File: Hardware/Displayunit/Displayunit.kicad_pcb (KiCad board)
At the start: 4 copper layers, 155 x 64.8 mm, 112 parts, among them IC1 TSC2007, IC2 MX25LM51245GXDI00, IC3 IS66WVH8M8BLL-100B1LI_0, J1 8P8C_Shielded, J2 8P8C_Shielded, J3 54104-4031, J4 Conn_ARM_JTAG_SWD_20, J5 52271-0679, J6 Conn_02x06_Odd_Even, J7 734-264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

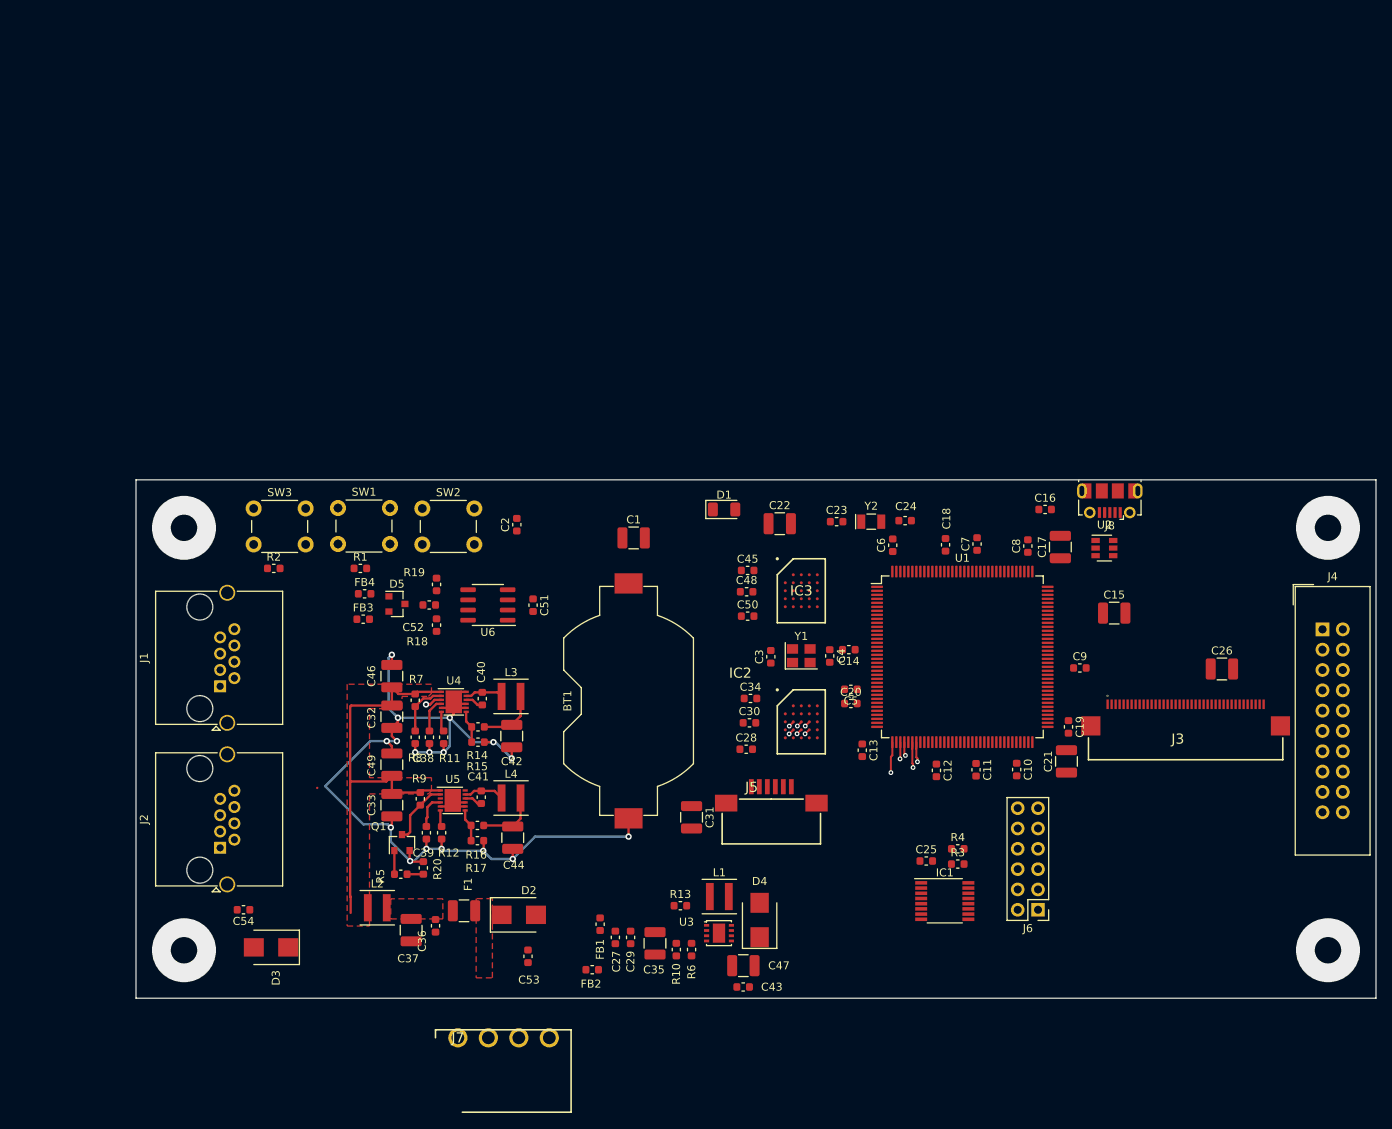
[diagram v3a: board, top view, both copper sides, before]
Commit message: Displayboard: Flex Stecker Position festgelegt, verschiebung von Componenten.
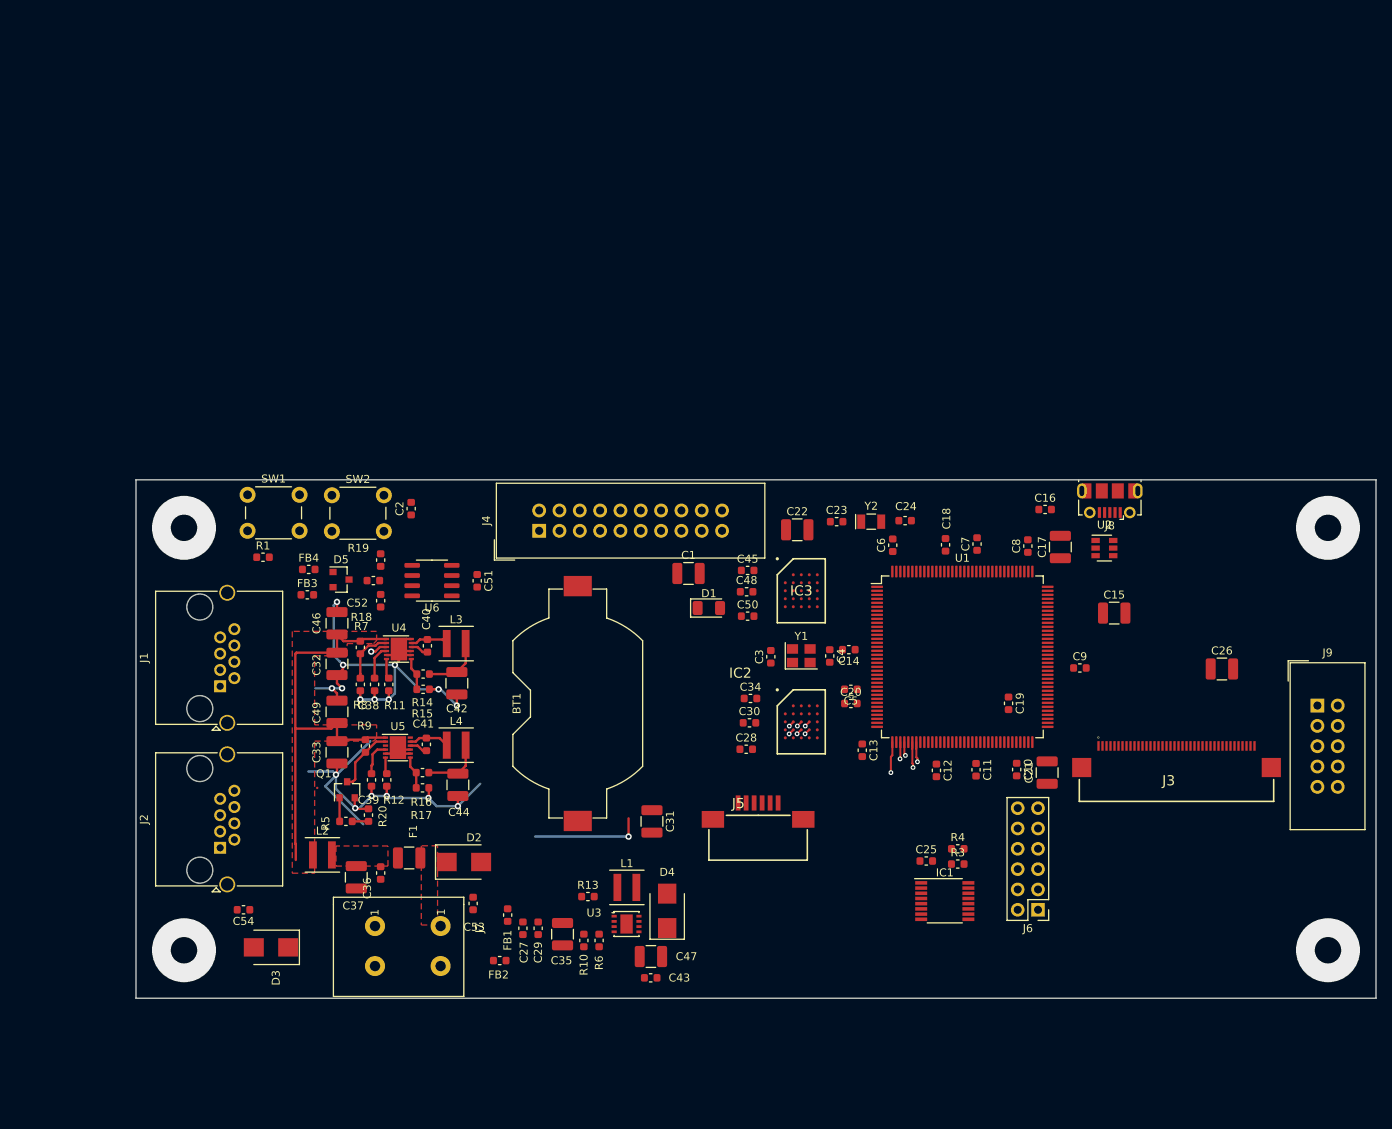
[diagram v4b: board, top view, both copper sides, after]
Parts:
- removed R2: 10K, Resistor_SMD:R_0603_1608Metric
- removed SW3: Wakeup, Button_Switch_THT:SW_PUSH_6mm_H8.5mm
- added J9: Conn_02x05_Odd_Even, Connector_IDC:IDC-Header_2x05_P2.54mm_Vertical, F.Cu at (209.7, 77.2)
- J7: value 734-264 -> WAGO_Klemmleiste_2-pol; footprint WAGO:SHDR4W120P0X381_1X4_1640X1030X850P -> WAGO:WAGO_Klemmleiste_Hebel4mm²Horizontal_RM5mm_2-pol
- moved J4 98.7 mm to (112.4, 55.4), turned to 90 degrees
- moved J7 14.1 mm to (100.1, 104.8), turned to 270 degrees
- moved C2 13.4 mm to (96.4, 52.6)
- moved D1 12.5 mm to (133.6, 65.0)
- moved R1 12.2 mm to (77.9, 58.7)
- moved C47 11.6 mm to (126.4, 108.6)
- moved D4 11.6 mm to (128.4, 102.9)
- moved C27 11.6 mm to (110.4, 105.1)
- moved C29 11.6 mm to (112.3, 105.1)
- moved C35 11.6 mm to (115.3, 105.8)
- moved C43 11.6 mm to (126.3, 111.3)
- moved FB1 11.6 mm to (108.5, 103.4)
- moved FB2 11.6 mm to (107.5, 109.1)
- moved L1 11.6 mm to (123.4, 99.9)
- moved R13 11.6 mm to (118.5, 101.1)
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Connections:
- J7 pad 2: Net-(C53-Pad1) -> GND

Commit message: Displayboard: Layout
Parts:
- added C55: 1uF, Capacitor_SMD:C_1210_3225Metric, F.Cu at (212.9, 68.7)
- added C56: 100n, Capacitor_SMD:C_0603_1608Metric, F.Cu at (202.1, 62.2)
- added FB10: 100R, Inductor_SMD:L_0603_1608Metric, F.Cu at (209.0, 70.2)
- added FB5: 100R, Inductor_SMD:L_0603_1608Metric, F.Cu at (202.5, 71.9)
- added FB6: 100R, Inductor_SMD:L_0603_1608Metric, F.Cu at (202.5, 73.8)
- added FB7: 100R, Inductor_SMD:L_0603_1608Metric, F.Cu at (202.5, 75.7)
- added FB8: 100R, Inductor_SMD:L_0603_1608Metric, F.Cu at (202.5, 77.6)
- added FB9: 100R, Inductor_SMD:L_0603_1608Metric, F.Cu at (202.5, 79.5)
- added U7: AT25xxx, Package_SO:SO-8_3.9x4.9mm_P1.27mm, F.Cu at (200.3, 66.2)
- moved D1 22.8 mm to (152.0, 51.6)
- moved C26 17.9 mm to (181.2, 79.5), turned to 180 degrees
- moved R3 16.6 mm to (149.7, 89.9), turned to 270 degrees
- moved R4 13.7 mm to (152.0, 89.9), turned to 270 degrees
- moved C50 12.9 mm to (147.3, 56.6)
- moved C31 12.1 mm to (136.9, 85.5), turned to 0 degrees
- moved C45 11.9 mm to (150.2, 61.9), turned to 90 degrees
- moved C28 9.20 mm to (146.7, 86.4)
- moved C19 8.46 mm to (177.8, 82.1), turned to 90 degrees
- moved IC1 8.14 mm to (159.1, 94.6), turned to 180 degrees
- moved C24 7.56 mm to (150.6, 54.9), turned to 270 degrees
- moved C3 7.12 mm to (148.5, 70.9), turned to 270 degrees
- moved C4 6.86 mm to (141.9, 70.8), turned to 90 degrees
- moved C30 6.70 mm to (142.9, 74.2), turned to 180 degrees
- moved J6 4.82 mm to (170.0, 103.5)
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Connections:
- net *I2C4_SCL renamed I2C4_SCL
- net *I2C4_SDA renamed I2C4_SDA
- net *LCD_BL_CTR renamed LCD_BL_CTR
- IC1 pad 11: I2C3_SDA -> I2C2_SDA
- IC1 pad 12: I2C3_SCL -> I2C2_SCL
- J3 pad 1: *LCD_LED-K -> LCD_LED-K
- J3 pad 2: *LCD_LED-A -> LCD_LED-A
- J5 pad 3: I2C3_SCL -> I2C2_SCL
- J5 pad 4: I2C3_SDA -> I2C2_SDA
- J6 pad 1: I2C3_SCL -> I2C2_SCL
- J6 pad 3: I2C3_SDA -> I2C2_SDA
- J9 pad 10: Net-(J9-Pad10) -> GND
- J9 pad 2: Net-(J9-Pad2) -> Net-(C55-Pad1)
- J9 pad 4: Net-(J9-Pad4) -> Net-(C55-Pad1)
- J9 pad 6: Net-(J9-Pad6) -> GND
- J9 pad 8: Net-(J9-Pad8) -> GND
- R3 pad 2: I2C3_SCL -> I2C2_SCL
- R4 pad 2: I2C3_SDA -> I2C2_SDA
- U1 pad 101: LCD_INT -> TOUCH_RESET
- U1 pad 136: Net-(U1-Pad136) -> USART1_TX
- U1 pad 137: Net-(U1-Pad137) -> USART1_RX
- U1 pad 139: Net-(U1-Pad139) -> EXT_1
- U1 pad 140: Net-(U1-Pad140) -> EXT_2
- U1 pad 65: Net-(U1-Pad65) -> EXT_3
- U1 pad 70: *I2C2_SCL -> I2C2_SCL
- U1 pad 71: *I2C2_SDA -> I2C2_SDA
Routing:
- net GND: track 128.8 -> 478.6 mm, vias 18 -> 64
- net +3V3: track 7.55 -> 202.8 mm, vias 0 -> 22
- net +3.3VA: track 7.64 -> 87.6 mm, vias 0 -> 4
- net TOUCH_INT: track 0.00 -> 79.4 mm, vias 0 -> 4
- net I2C2_SCL: track 0.00 -> 78.3 mm, vias 0 -> 4
- net TOUCH_RESET: track 0.00 -> 71.5 mm, vias 0 -> 2
- net LCD_LED-K: track 0.00 -> 69.4 mm, vias 0 -> 1
- net LCD_LED-A: track 0.00 -> 68.8 mm, vias 0 -> 1
- net I2C2_SDA: track 0.00 -> 62.6 mm, vias 0 -> 5
- net LCD_VSYNC: track 0.00 -> 55.4 mm, vias 0 -> 4
- net LCD_HSYNC: track 0.00 -> 54.4 mm, vias 0 -> 4
- net LCD_B0: track 0.00 -> 52.9 mm, vias 0 -> 2
- net LCD_R1: track 0.00 -> 51.1 mm, vias 0 -> 2
- net LCD_R0: track 0.00 -> 50.5 mm, vias 0 -> 2
- net LCD_G1: track 0.00 -> 50.5 mm, vias 0 -> 2
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
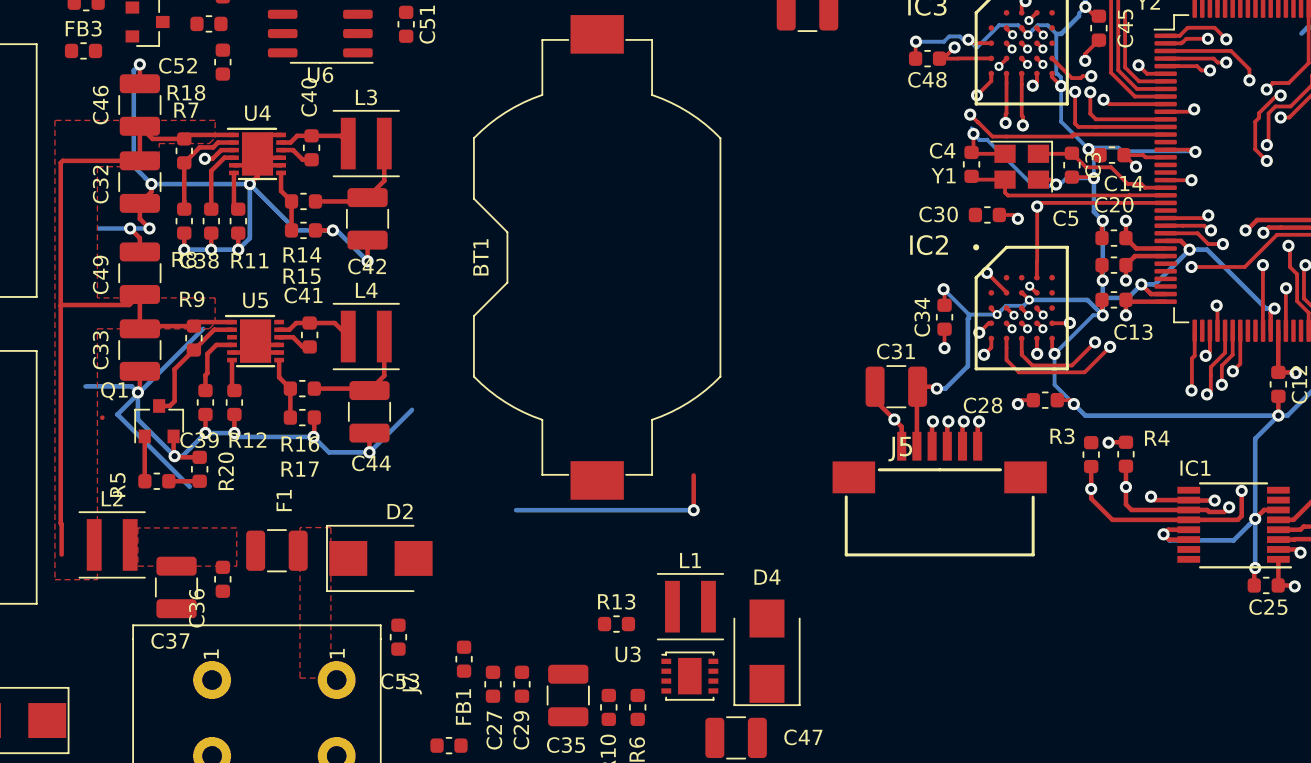
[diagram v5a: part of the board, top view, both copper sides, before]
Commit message: Weitere Arbeiten am Layout, UID i2c Eeprom hinzugefügt.
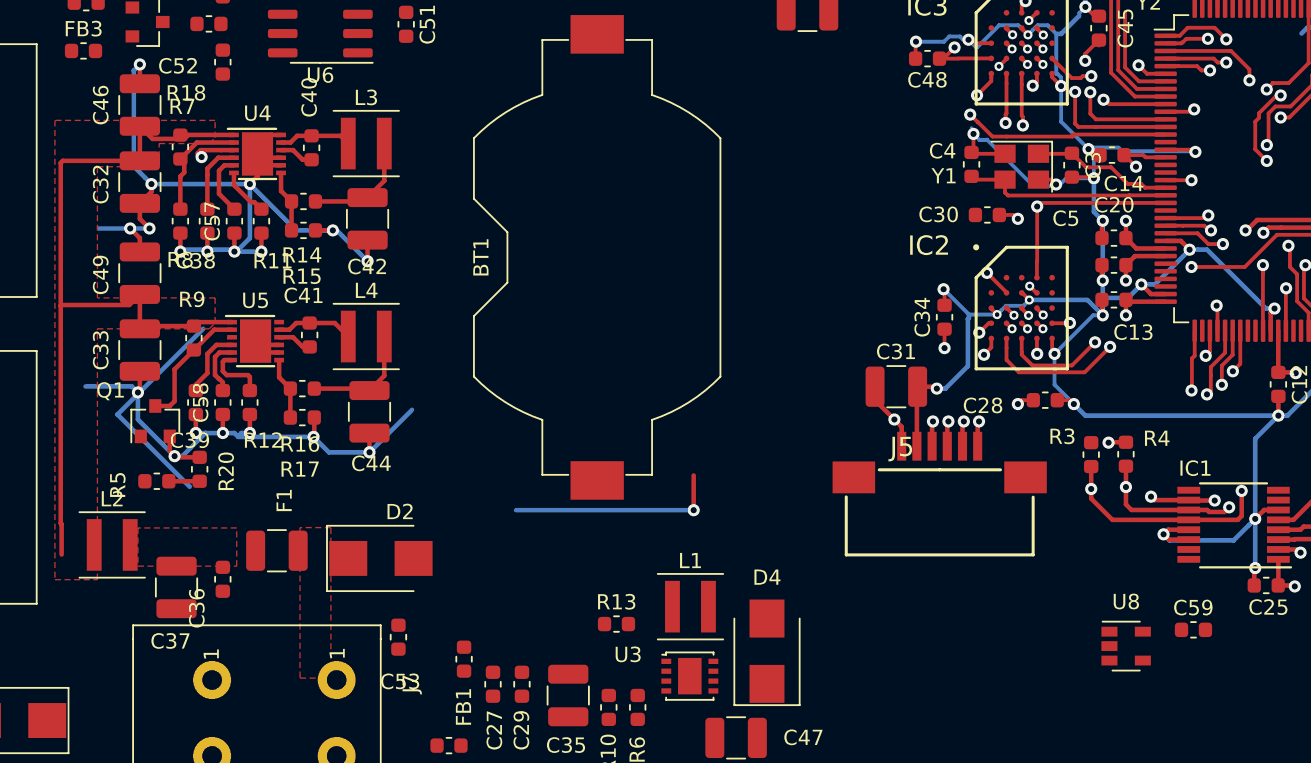
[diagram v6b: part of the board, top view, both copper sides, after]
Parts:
- added C57: 4u7, Capacitor_SMD:C_0603_1608Metric, F.Cu at (93.3, 74.6)
- added C58: 4u7, Capacitor_SMD:C_0603_1608Metric, F.Cu at (92.6, 86.5)
- added C59: 100n, Capacitor_SMD:C_0603_1608Metric, F.Cu at (156.5, 101.5)
- added U8: 24AA02-OT, Package_TO_SOT_SMD:SOT-23-5, F.Cu at (152.0, 102.5)
- moved R11 1.52 mm to (95.1, 74.6)
- moved R12 1.02 mm to (94.4, 86.5)
- moved C39 0.63 mm to (90.8, 86.5)
- moved R7 0.36 mm to (89.8, 69.7)
- moved C38 0.25 mm to (91.6, 74.6)
- moved R8 0.25 mm to (89.8, 74.6)
- moved Q1 0.25 mm to (88.1, 87.7)
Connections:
- U4 pad 5: GND -> Net-(C57-Pad2)
- U5 pad 5: GND -> Net-(C58-Pad2)
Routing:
- net GND: track 478.6 -> 483.3 mm, vias 64 -> 66
- net Net-(C57-Pad2): track 0.00 -> 4.08 mm
- net Net-(C58-Pad2): track 0.00 -> 3.68 mm
- net Net-(Q1-Pad1): track 2.96 -> 0.01 mm
- net Net-(R12-Pad1): track 2.07 -> 4.11 mm
- net Net-(R11-Pad1): track 2.50 -> 3.26 mm
